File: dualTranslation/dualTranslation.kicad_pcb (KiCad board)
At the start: 4 copper layers, 39.4 x 39.2 mm, 22 parts, among them IC1 LSF0108PWR, IC2 LSF0108PWR, IC3 TLV61225DC, J1 L_dual, J2 R_dual, J6 MISC

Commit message: pcb
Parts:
- added D1: RB751V40T1G, Diode_SMD:D_SOD-323, F.Cu at (143.1, 97.1)
- added D2: RB751V40T1G, Diode_SMD:D_SOD-323, F.Cu at (143.5, 103.3)
- added R10: 10K, Resistor_SMD:R_0402_1005Metric, F.Cu at (129.5, 86.5)
- added R11: 10K, Resistor_SMD:R_0402_1005Metric, F.Cu at (131.5, 95.0)
- added R12: 10K, Resistor_SMD:R_0402_1005Metric, F.Cu at (131.5, 93.8)
- added R13: 10K, Resistor_SMD:R_0402_1005Metric, F.Cu at (131.4, 92.6)
- added R14: 10K, Resistor_SMD:R_0402_1005Metric, F.Cu at (129.5, 84.0)
- added R16: 10K, Resistor_SMD:R_0402_1005Metric, F.Cu at (131.4, 91.4)
- added R17: 10K, Resistor_SMD:R_0402_1005Metric, F.Cu at (131.4, 90.3)
- added R18: 10K, Resistor_SMD:R_0402_1005Metric, F.Cu at (131.4, 89.1)
- added R19: 10K, Resistor_SMD:R_0402_1005Metric, F.Cu at (131.4, 88.0)
- added R20: 10K, Resistor_SMD:R_0402_1005Metric, F.Cu at (127.2, 80.5)
- added R21: 10K, Resistor_SMD:R_0402_1005Metric, F.Cu at (127.2, 89.2)
- added R22: 10K, Resistor_SMD:R_0402_1005Metric, F.Cu at (105.3, 93.6)
- added R23: 10K, Resistor_SMD:R_0402_1005Metric, F.Cu at (129.6, 81.5)
- added R24: 10K, Resistor_SMD:R_0402_1005Metric, F.Cu at (143.4, 95.0)
- added R25: 10K, Resistor_SMD:R_0402_1005Metric, F.Cu at (143.4, 92.7)
- added R26: 10K, Resistor_SMD:R_0402_1005Metric, F.Cu at (143.4, 90.3)
- added R27: 10K, Resistor_SMD:R_0402_1005Metric, F.Cu at (143.4, 87.8)
- added R28: 10K, Resistor_SMD:R_0402_1005Metric, F.Cu at (127.2, 81.8)
- added R29: 10K, Resistor_SMD:R_0402_1005Metric, F.Cu at (127.2, 85.5)
- added R3: 10K, Resistor_SMD:R_0402_1005Metric, F.Cu at (129.5, 85.3)
- added R30: 10K, Resistor_SMD:R_0402_1005Metric, F.Cu at (127.2, 86.8)
- added R31: 10K, Resistor_SMD:R_0402_1005Metric, F.Cu at (129.6, 80.2)
- added R32: 10K, Resistor_SMD:R_0402_1005Metric, F.Cu at (143.4, 93.9)
- added R33: 10K, Resistor_SMD:R_0402_1005Metric, F.Cu at (143.4, 91.5)
- added R34: 10K, Resistor_SMD:R_0402_1005Metric, F.Cu at (143.4, 89.0)
- added R35: 10K, Resistor_SMD:R_0402_1005Metric, F.Cu at (143.4, 86.4)
- added R4: 10K, Resistor_SMD:R_0402_1005Metric, F.Cu at (127.2, 90.5)
- added R5: 10K, Resistor_SMD:R_0402_1005Metric, F.Cu at (127.2, 84.3)
- added R6: 10K, Resistor_SMD:R_0402_1005Metric, F.Cu at (127.2, 88.0)
- added R7: 10K, Resistor_SMD:R_0402_1005Metric, F.Cu at (127.2, 83.0)
- added R8: 10K, Resistor_SMD:R_0402_1005Metric, F.Cu at (129.5, 82.8)
- added R9: 10K, Resistor_SMD:R_0402_1005Metric, F.Cu at (129.5, 87.7)
- C13, C14: footprint Capacitor_SMD:C_0603_1608Metric -> Capacitor_SMD:C_0402_1005Metric
- moved C2 23.3 mm to (104.7, 95.9)
- moved C3 23.3 mm to (104.7, 97.9)
- moved C4 23.3 mm to (104.7, 99.9)
- moved R1 23.3 mm to (104.7, 105.8)
- moved C5 23.3 mm to (104.7, 101.8)
- moved R2 23.3 mm to (104.7, 107.8)
- moved C1 23.2 mm to (104.6, 103.7)
- moved IC1 6.03 mm to (122.0, 91.1)
- moved IC2 3.80 mm to (136.7, 91.1)
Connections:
- C1 pad 1: /NB_A8 -> Net-(D2-K)
- C2 pad 1: /NB_B8 -> Net-(D1-K)
- IC1 pad 19: +3V3 -> Net-(D2-K)
- IC1 pad 20: /NB_A8 -> Net-(D2-K)
- IC2 pad 19: +3V3 -> Net-(D1-K)
- IC2 pad 20: /NB_B8 -> Net-(D1-K)
- R1 pad 1: +2V5 -> +3V3
- R1 pad 2: /NB_A8 -> Net-(D2-K)
- R2 pad 1: +2V5 -> +3V3
- R2 pad 2: /NB_B8 -> Net-(D1-K)
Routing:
- net GND: track 2.62 -> 84.8 mm, vias 4 -> 5
- net +3.3V: track 0.00 -> 29.3 mm
- net /NB_A7: track 0.00 -> 22.8 mm, vias 0 -> 1
- net /B4: track 0.00 -> 21.0 mm
- net /A4: track 0.00 -> 19.7 mm
- net /NB_B7: track 0.00 -> 18.8 mm, vias 0 -> 1
- net /B5: track 0.00 -> 17.9 mm
- net /B0: track 0.00 -> 17.0 mm
- net /A5: track 0.00 -> 16.3 mm
- net /B1: track 0.00 -> 15.9 mm
- net /B6: track 0.00 -> 15.6 mm
- net /NB_B6: track 0.00 -> 15.5 mm, vias 0 -> 1
- net /NB_A3: track 0.00 -> 15.5 mm, vias 0 -> 1
- net /NB_A2: track 0.00 -> 14.8 mm, vias 0 -> 1
- net /B2: track 0.00 -> 14.6 mm
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
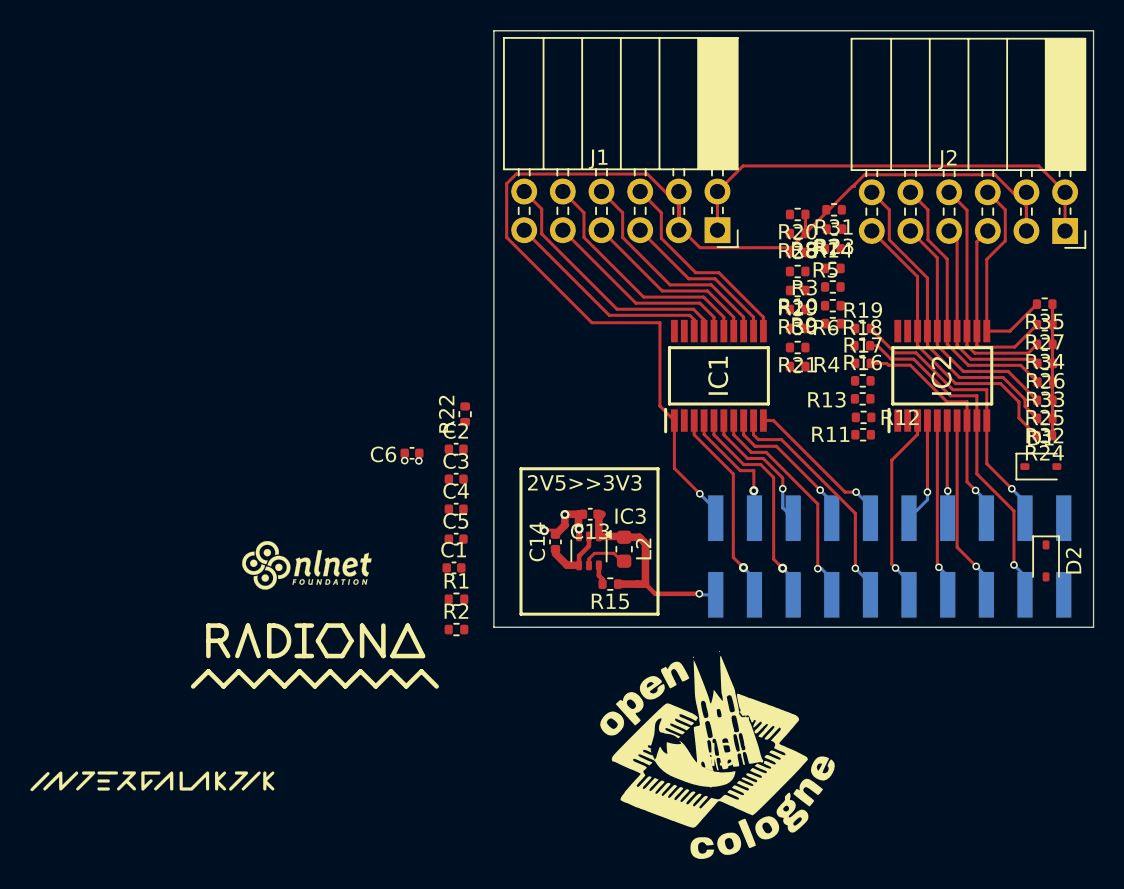
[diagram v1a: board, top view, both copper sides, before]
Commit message: Routing dualTranslarion
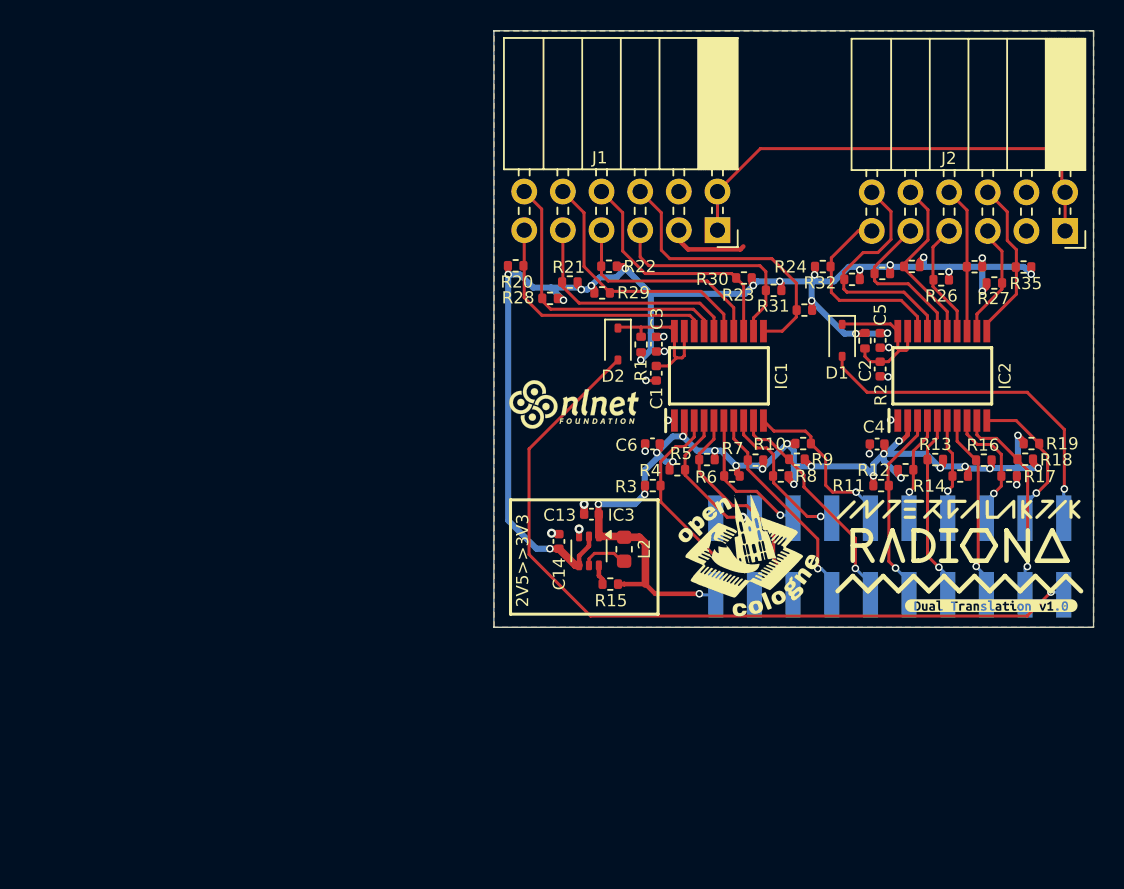
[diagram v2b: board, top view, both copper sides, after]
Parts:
- added kibuzzard-6749EA83: G***, kibuzzard-6749EA83, F.Cu at (139.9, 106.2)
- moved H1 55.9 mm to (137.8, 99.8)
- moved H4 42.8 mm to (137.8, 102.3)
- moved R2 32.9 mm to (131.6, 88.8), turned to -90 degrees
- moved D2 31.5 mm to (115.3, 89.0)
- moved C5 30.8 mm to (132.6, 88.8), turned to 90 degrees
- moved C2 28.4 mm to (132.6, 90.7), turned to -90 degrees
- moved C4 28.0 mm to (132.4, 95.6)
- moved R1 20.7 mm to (116.9, 89.0), turned to 90 degrees
- moved H2 20.5 mm to (112.5, 93.0)
- moved R20 18.8 mm to (108.6, 83.9), turned to 0 degrees
- moved C1 18.4 mm to (117.9, 90.9), turned to -90 degrees
- moved R24 18.3 mm to (128.8, 83.9), turned to 0 degrees
- moved R3 17.6 mm to (117.6, 98.3)
- moved R28 16.8 mm to (110.9, 86.0)
- moved R14 16.0 mm to (137.8, 97.7), turned to 180 degrees
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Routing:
- net +3V3: track 13.6 -> 90.7 mm, vias 0 -> 21
- net GND: track 84.8 -> 11.3 mm, vias 5 -> 11
- net +2V5: track 14.8 -> 74.8 mm, vias 2 -> 22
- net /NB_A8: track 0.00 -> 52.7 mm, vias 0 -> 1
- net /NB_B8: track 0.00 -> 22.9 mm, vias 0 -> 1
- net Net-(D1-K): track 0.00 -> 10.2 mm
- net Net-(D2-K): track 0.00 -> 10.0 mm
- net /NB_A7: track 22.8 -> 13.5 mm
- net /NB_B7: track 18.8 -> 9.84 mm
- net /NB_B6: track 15.5 -> 8.30 mm
- net /A4: track 19.7 -> 12.9 mm
- net /B5: track 17.9 -> 11.5 mm
- net /B6: track 15.6 -> 9.61 mm
- net /A5: track 16.3 -> 10.5 mm
- net /A6: track 13.5 -> 7.68 mm
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- added copper zone on B.Cu, net GND
- added copper zone on F.Cu, net GND
- added copper zone on In1.Cu, net GND
- added copper zone on In2.Cu, net GND
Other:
- board text added: "PCB3D_BR_DualTranslation"
- board text added: "PCB3D_TL_DualTranslation"
- board text removed: "PCB3D_BR_pwrIO"
- board text removed: "PCB3D_TL_pwrIO"
